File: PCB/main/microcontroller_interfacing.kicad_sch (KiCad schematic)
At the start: 11 parts, among them IC2 LM358DT, IC3 AT24C256C-SSHL-T, J9 PZ254V-11-02P

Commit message: created BOM
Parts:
- C11, C12: Comment (none) -> 3.3uF; JLCPCB Part (none) -> C51412; LCSC (none) -> C51412; Price($) (none) -> 0.0136
- C13: Comment (none) -> 100nF; JLCPCB Part Number (none) -> C14663; LCSC (none) -> C14663; Price($) (none) -> 0.0025
- IC2: Comment (none) -> LM358DT; JLCPCB Part Number C9418 -> C9481; LCSC (none) -> C9481; Price($) (none) -> 0.1043
- IC3: Comment (none) -> EEEPROM; JLCPCB Part (none) -> C6482; LCSC (none) -> C6482; Price($) (none) -> 1.5556
- J9: Comment (none) -> 2 pin male header; JLCPCB Part Number (none) -> C492401; LCSC (none) -> C492401; Price($) (none) -> 0.0106
- R12, R13: Comment (none) -> 1k; LCSC (none) -> C22548; Price($) (none) -> 0.0013
- TP8, TP9: Comment (none) -> test point; JLCPCB Part Number (none) -> C238130; LCSC (none) -> C238130; Price($) (none) -> 0.4796
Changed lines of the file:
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@@
+      (effects (font (size 1.27 1.27)) hide)
+    )
+    (property "Comment" "3.3uF" (id 14) (at 78.74 85.09 0)
+      (effects (font (size 1.27 1.27)) hide)
+    )
+    (property "JLCPCB Part" "C51412" (id 15) (at 78.74 85.09 0)
+      (effects (font (size 1.27 1.27)) hide)
+    )
+    (property "LCSC" "C51412" (id 16) (at 78.74 85.09 0)
+      (effects (font (size 1.27 1.27)) hide)
+    )
+    (property "Price($)" "0.0136" (id 17) (at 78.74 85.09 0)
       (effects (font (size 1.27 1.27)) hide)
     )
@@
     (property "Arrow Price/Stock" "" (id 11) (at 113.03 49.53 0)
       (effects (font (size 1.27 1.27)) (justify left) hide)
+    )
+    (property "Comment" "test point" (id 12) (at 92.71 66.04 0)
+      (effects (font (size 1.27 1.27)) hide)
+    )
+    (property "JLCPCB Part Number" "C238130" (id 13) (at 92.71 66.04 0)
+      (effects (font (size 1.27 1.27)) hide)
+    )
+    (property "LCSC" "C238130" (id 14) (at 92.71 66.04 0)
+      (effects (font (size 1.27 1.27)) hide)
+    )
+    (property "Price($)" "0.4796" (id 15) (at 92.71 66.04 0)
+      (effects (font (size 1.27 1.27)) hide)
     )
     (pin "1")
@@
     )
     (property "Price" "$0.0012" (id 13) (at 60.96 59.69 0)
+      (effects (font (size 1.27 1.27)) hide)
+    )
+    (property "Comment" "1k" (id 14) (at 60.96 59.69 0)
+      (effects (font (size 1.27 1.27)) hide)
+    )
+    (property "LCSC" "C22548" (id 15) (at 60.96 59.69 0)
+      (effects (font (size 1.27 1.27)) hide)
+    )
+    (property "Price($)" "0.0013" (id 16) (at 60.96 59.69 0)
       (effects (font (size 1.27 1.27)) hide)
     )
@@
       (effects (font (size 1.27 1.27)) (justify left) hide)
     )
-    (property "JLCPCB Part Number" "C9418" (id 12) (at 93.98 73.66 0)
+    (property "JLCPCB Part Number" "C9481" (id 12) (at 93.98 73.66 0)
       (effects (font (size 1.27 1.27)) hide)
     )
     (property "Price" "$0.1043" (id 13) (at 93.98 73.66 0)
+      (effects (font (size 1.27 1.27)) hide)
+    )
+    (property "Comment" "LM358DT" (id 14) (at 93.98 73.66 0)
+      (effects (font (size 1.27 1.27)) hide)
+    )
+    (property "LCSC" "C9481" (id 15) (at 93.98 73.66 0)
+      (effects (font (size 1.27 1.27)) hide)
+    )
+    (property "Price($)" "0.1043" (id 16) (at 93.98 73.66 0)
       (effects (font (size 1.27 1.27)) hide)
     )
@@
       (effects (font (size 1.27 1.27)) (justify left) hide)
     )
+    (property "Comment" "test point" (id 12) (at 121.92 73.66 0)
+      (effects (font (size 1.27 1.27)) hide)
+    )
+    (property "JLCPCB Part Number" "C238130" (id 13) (at 121.92 73.66 0)
+      (effects (font (size 1.27 1.27)) hide)
+    )
+    (property "LCSC" "C238130" (id 14) (at 121.92 73.66 0)
+      (effects (font (size 1.27 1.27)) hide)
+    )
+    (property "Price($)" "0.4796" (id 15) (at 121.92 73.66 0)
+      (effects (font (size 1.27 1.27)) hide)
+    )
     (pin "1")
   )
@@
       (effects (font (size 1.27 1.27)) (justify left) hide)
     )
+    (property "Comment" "2 pin male header" (id 12) (at 236.22 43.18 0)
+      (effects (font (size 1.27 1.27)) hide)
+    )
+    (property "JLCPCB Part Number" "C492401" (id 13) (at 236.22 43.18 0)
+      (effects (font (size 1.27 1.27)) hide)
+    )
+    (property "LCSC" "C492401" (id 14) (at 236.22 43.18 0)
+      (effects (font (size 1.27 1.27)) hide)
+    )
+    (property "Price($)" "0.0106" (id 15) (at 236.22 43.18 0)
+      (effects (font (size 1.27 1.27)) hide)
+    )
     (pin "1")
     (pin "2")
@@
     (property "Arrow Price/Stock" "https://www.arrow.com/en/products/cc0603krx7r9bb104/yageo?region=nac" (id 11) (at 245.11 30.48 0)
       (effects (font (size 1.27 1.27)) (justify left) hide)
+    )
+    (property "Comment" "100nF" (id 12) (at 223.52 39.37 0)
+      (effects (font (size 1.27 1.27)) hide)
+    )
+    (property "JLCPCB Part Number" "C14663" (id 13) (at 223.52 39.37 0)
+      (effects (font (size 1.27 1.27)) hide)
+    )
+    (property "LCSC" "C14663" (id 14) (at 223.52 39.37 0)
+      (effects (font (size 1.27 1.27)) hide)
+    )
+    (property "Price($)" "0.0025" (id 15) (at 223.52 39.37 0)
+      (effects (font (size 1.27 1.27)) hide)
     )
     (pin "1")
@@
       (effects (font (size 1.27 1.27)) hide)
     )
+    (property "Comment" "3.3uF" (id 14) (at 59.69 85.09 0)
+      (effects (font (size 1.27 1.27)) hide)
+    )
+    (property "JLCPCB Part" "C51412" (id 15) (at 59.69 85.09 0)
+      (effects (font (size 1.27 1.27)) hide)
+    )
+    (property "LCSC" "C51412" (id 16) (at 59.69 85.09 0)
+      (effects (font (size 1.27 1.27)) hide)
+    )
+    (property "Price($)" "0.0136" (id 17) (at 59.69 85.09 0)
+      (effects (font (size 1.27 1.27)) hide)
+    )
     (pin "1")
     (pin "2")
@@
       (effects (font (size 1.27 1.27)) hide)
     )
+    (property "Comment" "1k" (id 14) (at 39.37 68.58 0)
+      (effects (font (size 1.27 1.27)) hide)
+    )
+    (property "LCSC" "C22548" (id 15) (at 39.37 68.58 0)
+      (effects (font (size 1.27 1.27)) hide)
+    )
+    (property "Price($)" "0.0013" (id 16) (at 39.37 68.58 0)
+      (effects (font (size 1.27 1.27)) hide)
+    )
     (pin "1")
     (pin "2")
@@
       (effects (font (size 1.27 1.27)) hide)
     )
+    (property "Comment" "EEEPROM" (id 14) (at 110.49 125.73 0)
+      (effects (font (size 1.27 1.27)) hide)
+    )
+    (property "JLCPCB Part" "C6482" (id 15) (at 110.49 125.73 0)
+      (effects (font (size 1.27 1.27)) hide)
+    )
+    (property "LCSC" "C6482" (id 16) (at 110.49 125.73 0)
+      (effects (font (size 1.27 1.27)) hide)
+    )
+    (property "Price($)" "1.5556" (id 17) (at 110.49 125.73 0)
+      (effects (font (size 1.27 1.27)) hide)
+    )

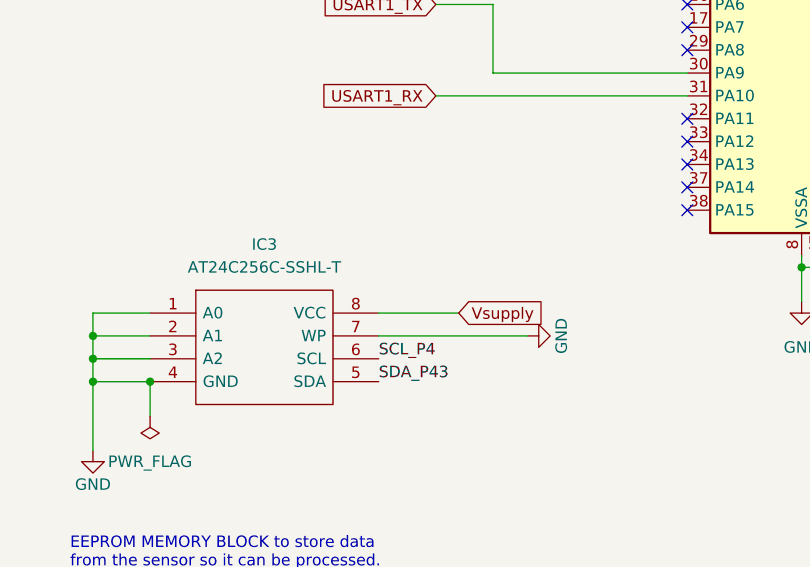
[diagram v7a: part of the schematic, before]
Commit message: modified power schematic
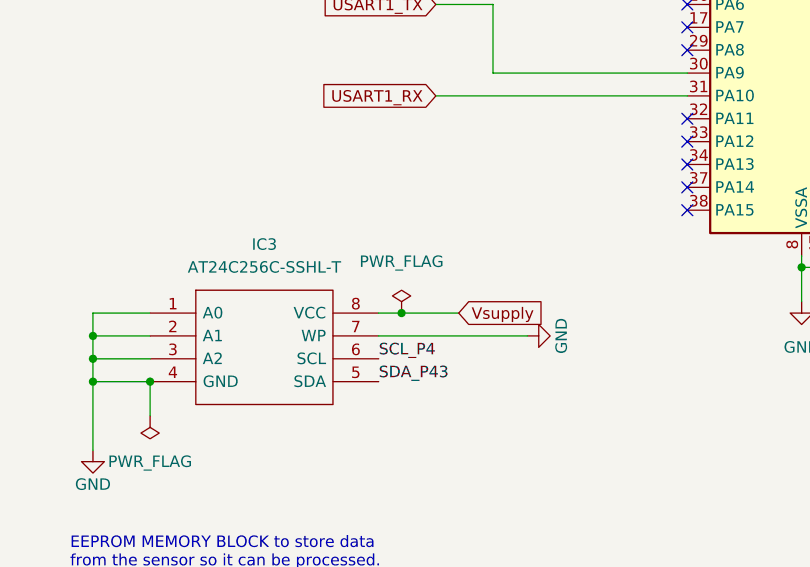
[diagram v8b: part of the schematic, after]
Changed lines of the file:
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@@
   (junction (at 104.14 128.27) (diameter 0) (color 0 0 0 0)
+  )
+  (junction (at 138.43 125.73) (diameter 0) (color 0 0 0 0)
   )
   (junction (at 87.63 73.66) (diameter 0) (color 0 0 0 0)
@@
     (stroke (width 0) (type default) (color 0 0 0 0))
   )
-  (wire (pts (xy 135.89 125.73) (xy 144.78 125.73))
+  (wire (pts (xy 135.89 125.73) (xy 138.43 125.73))
     (stroke (width 0) (type default) (color 0 0 0 0))
   )
@@
   )
   (wire (pts (xy 121.92 73.66) (xy 125.73 73.66))
+    (stroke (width 0) (type default) (color 0 0 0 0))
+  )
+  (wire (pts (xy 138.43 125.73) (xy 144.78 125.73))
     (stroke (width 0) (type default) (color 0 0 0 0))
   )
@@
       (effects (font (size 1.27 1.27)) hide)
     )
+    (pin "1")
+  )
+  (symbol (lib_id "power:PWR_FLAG") (at 138.43 125.73 0) (unit 1)
+    (in_bom yes) (on_board yes) (fields_autoplaced)
+    (property "Reference" "#FLG08" (id 0) (at 138.43 123.825 0)
+      (effects (font (size 1.27 1.27)) hide)
+    )
+    (property "Value" "PWR_FLAG" (id 1) (at 138.43 120.015 0))
+    (property "Footprint" "" (id 2) (at 138.43 125.73 0)
+      (effects (font (size 1.27 1.27)) hide)
+    )
+    (property "Datasheet" "~" (id 3) (at 138.43 125.73 0)
+      (effects (font (size 1.27 1.27)) hide)
+    )
